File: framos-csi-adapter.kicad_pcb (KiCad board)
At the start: 4 copper layers, 26.5 x 26.5 mm, 41 parts, among them J1 DF40C-60DS-0.4V(51), J2 MSAK24025P30, U1 NTS0102DP, U2 NCP163ASN330T1G

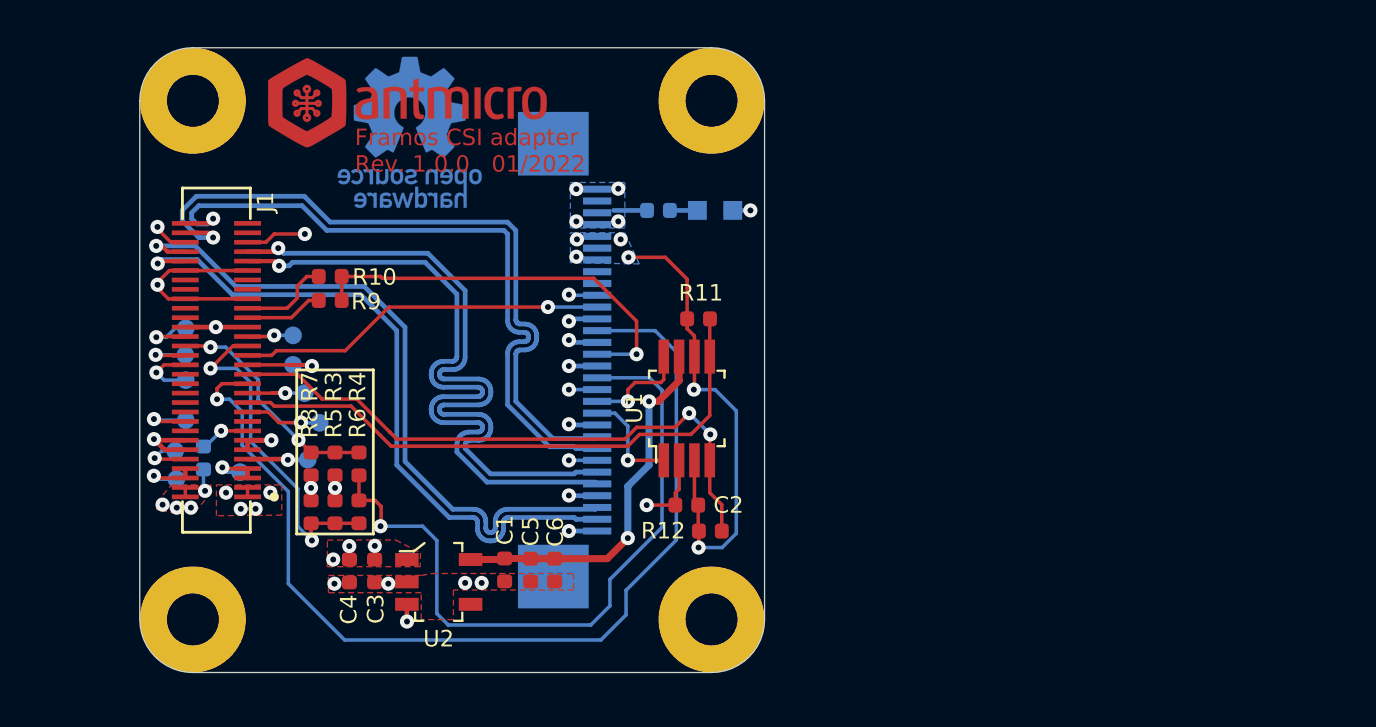
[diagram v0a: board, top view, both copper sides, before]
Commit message: Move R1 to top
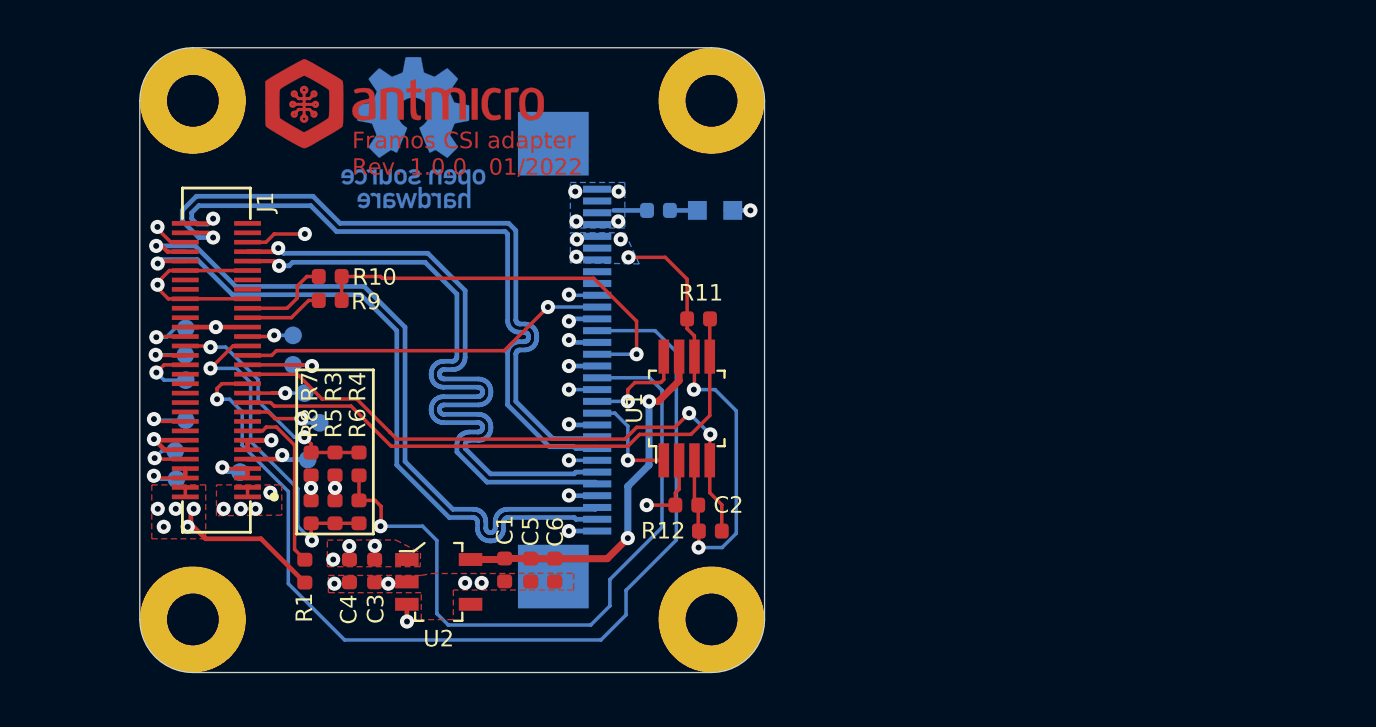
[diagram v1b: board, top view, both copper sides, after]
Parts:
- R1: moved to F.Cu
- moved R1 6.44 mm to (107.0, 122.2)
- moved N1 0.15 mm to (111.6, 103.6)
- moved N2 0.13 mm to (111.2, 102.4)
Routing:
- net 1V8_CAM: track 23.1 -> 28.7 mm, vias 11 -> 12
- net /XCLR: track 2.15 -> 7.42 mm, vias 1 -> 0

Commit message: Move power supply sections on PCB
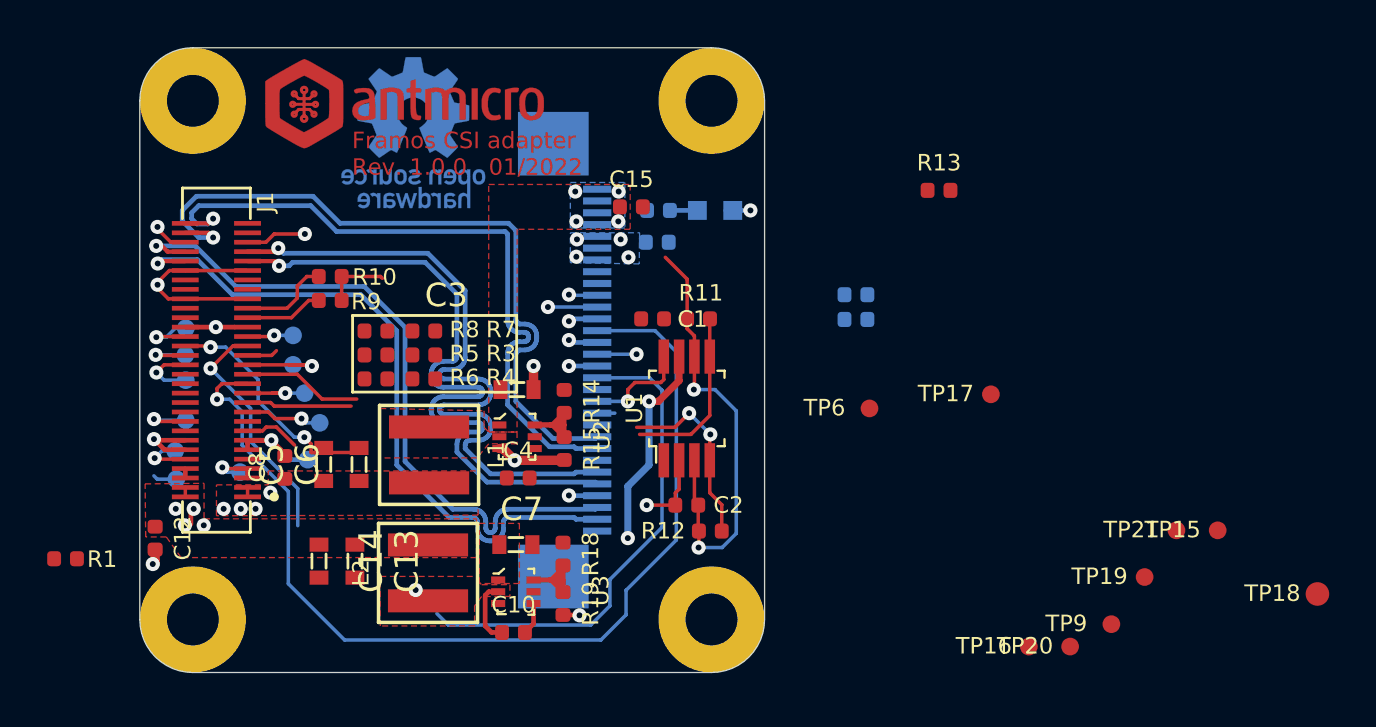
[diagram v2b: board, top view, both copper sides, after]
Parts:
- added C10: C_100n_0402, antmicro-footprints:0402-cap, F.Cu at (115.8, 124.8)
- added C12: C_100n_0402, framos-csi-adapter-footprints:0402-cap, F.Cu at (100.7, 120.8)
- added C13: C_22u_0603, antmicro-footprints:0603-cap, F.Cu at (109.1, 121.8)
- added C14: C_22u_0603, antmicro-footprints:0603-cap, F.Cu at (107.6, 121.8)
- added C15: C_100n_0402, framos-csi-adapter-footprints:0402-cap, F.Cu at (120.8, 106.8)
- added C16: C_100n_0402, framos-csi-adapter-footprints:0402-cap, B.Cu at (122.0, 108.2)
- added C7: C_22u_0603, antmicro-footprints:0603-cap, F.Cu at (116.0, 121.1)
- added C8: C_100n_0402, framos-csi-adapter-footprints:0402-cap, F.Cu at (106.2, 117.8)
- added L1: XEL4030-332MEC, antmicro-footprints:Coilcraft-XEL4030, F.Cu at (112.3, 117.3)
- added L2: XEL4030-222MEC, antmicro-footprints:Coilcraft-XEL4030, F.Cu at (112.2, 122.3)
- added R13: R_0R_0402, framos-csi-adapter-footprints:0402-res, F.Cu at (133.9, 106.0)
- added R14: R_14k7_0402, antmicro-footprints:0402-res, F.Cu at (118.0, 115.0)
- added R15: R_3k92_0402, antmicro-footprints:0402-res, F.Cu at (118.0, 117.0)
- added R16: R_0R_0402, antmicro-footprints:0402-res, B.Cu at (130.4, 110.5)
- added R17: R_0R_0402, antmicro-footprints:0402-res, B.Cu at (130.4, 111.5)
- added R18: R_12k4_0402, antmicro-footprints:0402-res, F.Cu at (118.0, 121.5)
- added R19: R_10k_0402, antmicro-footprints:0402-res, F.Cu at (118.0, 123.6)
- added TP15: TP_SMD_0_75MM, framos-csi-adapter-footprints:Testpoint_smd_0_75mm, F.Cu at (145.7, 120.5)
- added TP16: TP_SMD_0_75MM, framos-csi-adapter-footprints:Testpoint_smd_0_75mm, F.Cu at (137.7, 125.5)
- added TP17: TP_SMD_0_75MM, framos-csi-adapter-footprints:Testpoint_smd_0_75mm, F.Cu at (136.1, 114.8)
- added TP18: TP_SMD1MM, antmicro-footprints:Testpoint_smd_1mm, F.Cu at (149.9, 123.2)
- added TP19: TP_SMD_0_75MM, framos-csi-adapter-footprints:Testpoint_smd_0_75mm, F.Cu at (142.6, 122.5)
- added TP20: TP_SMD_0_75MM, framos-csi-adapter-footprints:Testpoint_smd_0_75mm, F.Cu at (139.5, 125.5)
- added TP21: TP_SMD_0_75MM, framos-csi-adapter-footprints:Testpoint_smd_0_75mm, F.Cu at (144.0, 120.5)
- added TP6: TP_SMD_0_75MM, framos-csi-adapter-footprints:Testpoint_smd_0_75mm, F.Cu at (130.9, 115.3)
- added TP9: TP_SMD_0_75MM, framos-csi-adapter-footprints:Testpoint_smd_0_75mm, F.Cu at (141.2, 124.5)
- added U3: AP62301Z6-7, antmicro-footprints:SOT-563, F.Cu at (116.0, 123.1)
- C3, C6: value C_1u_0402 -> C_22u_0603; footprint framos-csi-adapter-footprints:0402-cap -> antmicro-footprints:0603-cap
- C4: footprint framos-csi-adapter-footprints:0402-cap -> antmicro-footprints:0402-cap
- C5: value C_100n_0402 -> C_22u_0603; footprint framos-csi-adapter-footprints:0402-cap -> antmicro-footprints:0603-cap
- U2: value NCP163ASN330T1G -> AP62301Z6-7; footprint framos-csi-adapter-footprints:SOT-23-5 -> antmicro-footprints:SOT-563
- moved C1 12.4 mm to (121.8, 111.5), turned to 180 degrees
- moved R1 10.2 mm to (96.8, 121.7), turned to 180 degrees
- moved C5 9.86 mm to (107.8, 117.7), turned to 90 degrees
- moved C3 9.78 mm to (116.0, 114.5), turned to 0 degrees
- moved C6 9.43 mm to (109.3, 117.7), turned to 90 degrees
- moved C4 8.17 mm to (116.0, 118.2), turned to 0 degrees
- moved R8 8.15 mm to (110.0, 112.0), turned to 180 degrees
- moved R7 7.39 mm to (112.0, 112.0), turned to 180 degrees
- moved U2 7.00 mm to (116.0, 116.5)
- moved R5 6.88 mm to (110.0, 113.0), turned to 180 degrees
- moved R3 5.96 mm to (112.0, 113.0), turned to 180 degrees
- moved R6 5.68 mm to (110.0, 114.0), turned to 180 degrees
- moved R4 4.54 mm to (112.0, 114.0), turned to 0 degrees
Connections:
- C1 pad 1: 3V3 -> 3V3FFC
- C3 pad 1: 3V8_CAM -> 5V0_SYS
- C4 pad 1: 3V8_CAM -> Net-(C4-Pad1)
- C4 pad 2: GND -> Net-(C4-Pad2)
- C5 pad 1: 3V3 -> 3V8_CAM
- C6 pad 1: 3V3 -> 3V8_CAM
- J1 pad 16: Net-(J1-Pad16) -> (no net)
- J1 pad 17: Net-(J1-Pad17) -> (no net)
- J1 pad 20: Net-(J1-Pad20) -> (no net)
- J1 pad 22: Net-(J1-Pad22) -> (no net)
- J1 pad 24: Net-(J1-Pad24) -> (no net)
- J1 pad 26: Net-(J1-Pad26) -> (no net)
- J1 pad 28: Net-(J1-Pad28) -> (no net)
- J1 pad 40: Net-(J1-Pad40) -> (no net)
- J1 pad 42: Net-(J1-Pad42) -> (no net)
- J1 pad 45: Net-(J1-Pad45) -> (no net)
- J1 pad 46: Net-(J1-Pad46) -> CSI_D3_N
- J1 pad 47: Net-(J1-Pad47) -> (no net)
- J1 pad 48: Net-(J1-Pad48) -> CSI_D3_P
- J1 pad 57: Net-(J1-Pad57) -> CSI_D2_N
- J1 pad 59: Net-(J1-Pad59) -> CSI_D2_P
- J2 pad 11: CAM_SDA_3V3 -> CSI_D0_N
- J2 pad 12: CAM_SCL_3V3 -> CSI_D0_P
- J2 pad 14: CSI_CAM_EN -> CSI_CLK_N
- J2 pad 15: GND -> CSI_CLK_P
- J2 pad 16: CSI_CAM_CLK -> GND
- J2 pad 17: GND -> CAM_SDA_3V3
- J2 pad 18: CSI_CAM_XVS -> CAM_SCL_3V3
- J2 pad 2: CSI_D1_N -> CSI_D3_N
- J2 pad 20: CSI_CAM_XTRIG -> CSI_CAM_EN
- J2 pad 21: GND -> CSI_CAM_XVS
- J2 pad 22: Net-(J2-Pad22) -> CSI_CAM_CLK
- J2 pad 23: Net-(J2-Pad23) -> CSI_CAM_XTRIG
- J2 pad 24: 1V8_CAM -> 3V3FFC
- J2 pad 25: 1V8_CAM -> 3V3FFC
- J2 pad 26: 1V8_CAM -> 3V3FFC
- J2 pad 27: 3V8_CAM -> 5V0_SYS
- J2 pad 28: 3V8_CAM -> 5V0_SYS
- J2 pad 29: 3V8_CAM -> 5V0_SYS
- J2 pad 3: CSI_D1_P -> CSI_D3_P
- J2 pad 30: 3V8_CAM -> 5V0_SYS
- J2 pad 5: CSI_D0_N -> CSI_D2_N
- J2 pad 6: CSI_D0_P -> CSI_D2_P
- J2 pad 8: CSI_CLK_N -> CSI_D1_N
- J2 pad 9: CSI_CLK_P -> CSI_D1_P
- R10 pad 1: CSI_CAM_CLK -> Net-(R10-Pad1)
- R9 pad 1: CSI_CAM_CLK -> Net-(R10-Pad1)
- U1 pad 7: 3V3 -> 3V3FFC
- U2 pad 1: 3V8_CAM -> 5V0_SYS
- U2 pad 2: GND -> Net-(C4-Pad1)
- U2 pad 3: 3V8_CAM -> GND
- U2 pad 4: (no net) -> Net-(C4-Pad2)
- U2 pad 5: 3V3 -> Net-(TP6-Pad1)
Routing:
- net CSI_CAM_EN: track 29.6 -> 2.09 mm
- net 3V3: track 22.9 -> 0.00 mm, vias 2 -> 0
- net CSI_CLK_N: track 29.6 -> 50.5 mm
- net CSI_CAM_CLK: track 17.4 -> 0.00 mm, vias 1 -> 0
- net CSI_CAM_XTRIG: track 15.7 -> 1.31 mm, vias 1 -> 0
- net CAM_SCL_1V8: track 25.0 -> 11.9 mm
- net CAM_SDA_1V8: track 25.9 -> 13.1 mm
- net 3V3FFC: track 0.00 -> 8.84 mm, vias 0 -> 6
- net 1V8_CAM: track 28.7 -> 20.2 mm, vias 12 -> 6
- net Net-(R14-Pad2): track 0.00 -> 5.81 mm
- net /XCLR: track 7.42 -> 2.38 mm
- net Net-(R18-Pad2): track 0.00 -> 4.99 mm
- net /PW_EN_0: track 14.5 -> 10.2 mm, vias 2 -> 1
- net Net-(C10-Pad1): track 0.00 -> 3.44 mm, vias 0 -> 1
- net CAM_SDA_3V3: track 4.50 -> 1.24 mm
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- added copper zone on B.Cu, net 3V3FFC
- added copper zone on B.Cu, net 5V0_SYS
- added copper zone on F.Cu, net 5V0_SYS
- added copper zone on F.Cu, net Net-(C10-Pad1)
- added copper zone on F.Cu, net Net-(C4-Pad1)
- removed copper zone on B.Cu, net 1V8_CAM
- removed copper zone on B.Cu, net 3V8_CAM
- removed copper zone on F.Cu, net GND

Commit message: Layout, tunning
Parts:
- removed N1: oshw_logo, framos-csi-adapter-footprints:oshw-logo
- added REF**: OSHW-Logo2_7.3x6mm_Copper_Mask, framos-csi-adapter-footprints:OSHW-Logo2_7.3x6mm_Copper_Mask, F.Cu at (123.6, 119.0)
- added REF**: OSHW-Logo2_7.3x6mm_Copper, framos-csi-adapter-footprints:OSHW-Logo2_7.3x6mm_Copper, F.Cu at (123.6, 119.0)
- added REF**: MSAK24025P30_PLUG, framos-csi-adapter-footprints:MSAK24025P30_PLUG, F.Cu at (113.2, 114.1)
- added kibuzzard-621A77E1: G***, label, F.Cu at (102.0, 110.4)
- C10, C4: footprint antmicro-footprints:0402-cap -> framos-csi-adapter-footprints:0402-cap
- C12, C8, J1, MP1, MP2, MP3, MP4, R1, TP15, TP16: moved to B.Cu
- C13, C14, C3, C5, C6, C7: footprint antmicro-footprints:0603-cap -> framos-csi-adapter-footprints:0603-cap
- C16, D1, J2, R2: moved to F.Cu
- L1: value XEL4030-332MEC -> 74479887222C; footprint antmicro-footprints:Coilcraft-XEL4030 -> framos-csi-adapter-footprints:L_1008_2520Metric
- L2: value XEL4030-222MEC -> 74479887222C; footprint antmicro-footprints:Coilcraft-XEL4030 -> framos-csi-adapter-footprints:L_1008_2520Metric
- R14: value R_14k7_0402 -> R_37k4_0402; footprint antmicro-footprints:0402-res -> framos-csi-adapter-footprints:0402-res
- R15: value R_3k92_0402 -> R_10k_0402; footprint antmicro-footprints:0402-res -> framos-csi-adapter-footprints:0402-res
- R16, R17: footprint antmicro-footprints:0402-res -> framos-csi-adapter-footprints:0402-res; moved to F.Cu
- R18, R19: footprint antmicro-footprints:0402-res -> framos-csi-adapter-footprints:0402-res
- TP18: footprint antmicro-footprints:Testpoint_smd_1mm -> framos-csi-adapter-footprints:Testpoint_smd_1mm
- U2, U3: footprint antmicro-footprints:SOT-563 -> framos-csi-adapter-footprints:SOT-563
- moved TP9 42.0 mm to (102.7, 107.8)
- moved TP21 39.1 mm to (105.2, 114.9)
- moved TP18 37.1 mm to (112.9, 122.5), turned to 270 degrees
- moved TP15 34.4 mm to (114.5, 106.1)
- moved R13 32.6 mm to (101.3, 107.6), turned to 180 degrees
- moved TP20 32.6 mm to (108.7, 114.8)
- moved R1 31.8 mm to (121.4, 101.4), turned to 90 degrees
- moved TP16 31.5 mm to (112.8, 106.2)
- moved MP2 31.1 mm to (124.2, 102.2), turned to 270 degrees
- moved MP3 31.1 mm to (102.2, 124.2), turned to 270 degrees
- moved TP6 29.6 mm to (101.8, 120.3), turned to 270 degrees
- moved TP19 29.1 mm to (113.7, 125.8), turned to 270 degrees
- moved TP17 27.1 mm to (109.2, 117.7)
- moved C12 26.5 mm to (121.5, 104.4)
- moved TP11 24.4 mm to (118.5, 100.7), turned to 90 degrees
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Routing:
- net CSI_CAM_XVS: track 44.0 -> 12.6 mm, vias 2 -> 3
- net CSI_CLK_N: track 50.5 -> 23.5 mm
- net /PW_EN_1: track 9.98 -> 35.3 mm, vias 2 -> 3
- net CSI_D2_P: track 0.00 -> 24.0 mm, vias 0 -> 1
- net CSI_D2_N: track 0.00 -> 24.0 mm, vias 0 -> 1
- net CSI_D3_P: track 0.00 -> 23.5 mm, vias 0 -> 1
- net CSI_D3_N: track 0.00 -> 23.5 mm, vias 0 -> 1
- net /INCK: track 3.33 -> 18.7 mm, vias 0 -> 1
- net /MCLK1: track 3.88 -> 18.5 mm, vias 0 -> 1
- net CAM_SCL_3V3: track 4.48 -> 18.0 mm, vias 1 -> 0
- net CAM_SDA_3V3: track 1.24 -> 13.9 mm, vias 1 -> 2
- net CSI_CAM_XTRIG: track 1.31 -> 13.8 mm, vias 0 -> 1
- net CSI_CAM_CLK: track 0.00 -> 12.5 mm
- net CAM_SCL_1V8: track 11.9 -> 23.1 mm, vias 0 -> 1
- net 3V8_CAM: track 0.40 -> 10.1 mm, vias 4 -> 8
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- added copper zone on B.Cu, net 1V8_CAM
- added copper zone on F.Cu, net 3V3FFC
- added copper zone on B.Cu, net 3V8_CAM
- added copper zone on In1.Cu, net 5V0_SYS
- added copper zone on B.Cu, net GND
- added copper zone on F.Cu, net GND
- removed copper zone on B.Cu, net 3V3FFC
- removed copper zone on B.Cu, net 5V0_SYS
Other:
- board text added: "Framos CSI adapter Rev. 1.0.0 02/2022"
- board text removed: "Framos CSI adapter Rev. 1.0.0 01/2022"
- board text removed: "HOST"
- board text removed: "POWER"

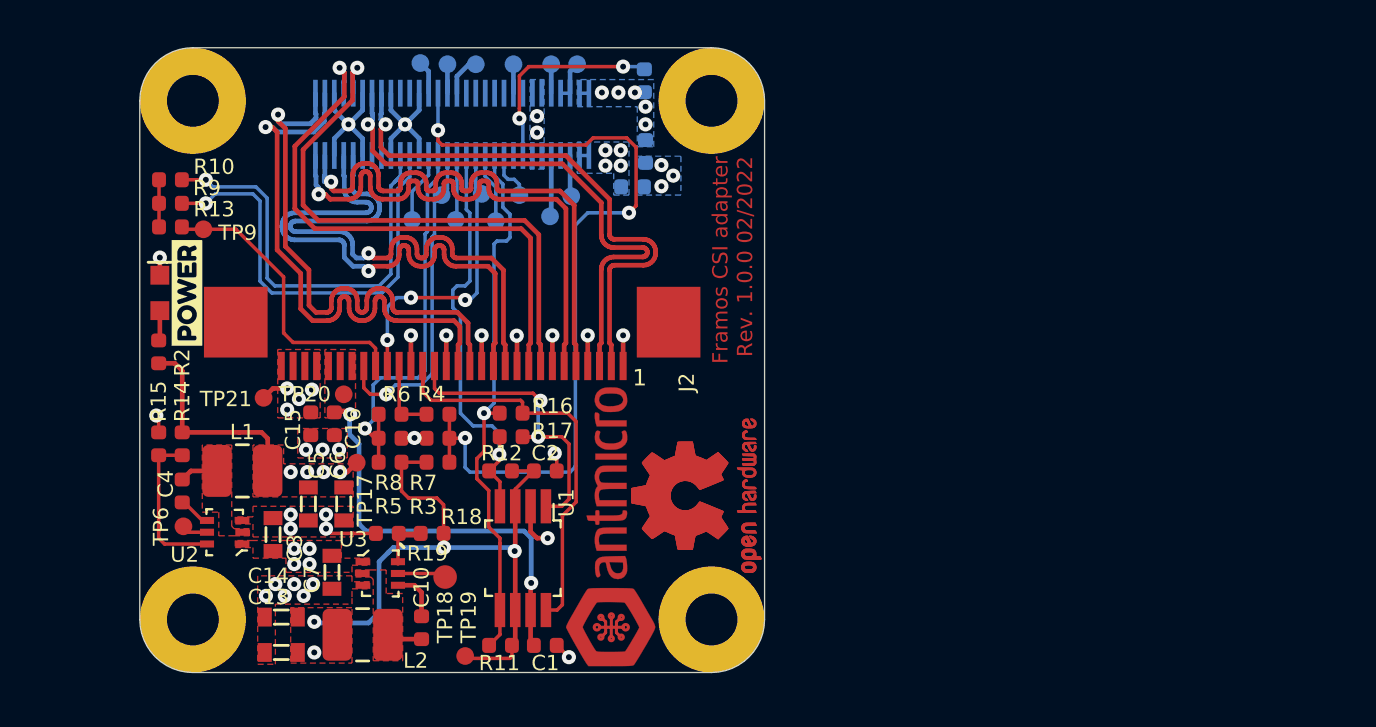
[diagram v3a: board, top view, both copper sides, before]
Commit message: Changed voltage translator to XSON8 package. Crossed P and N signals on D2 and D3 lanes
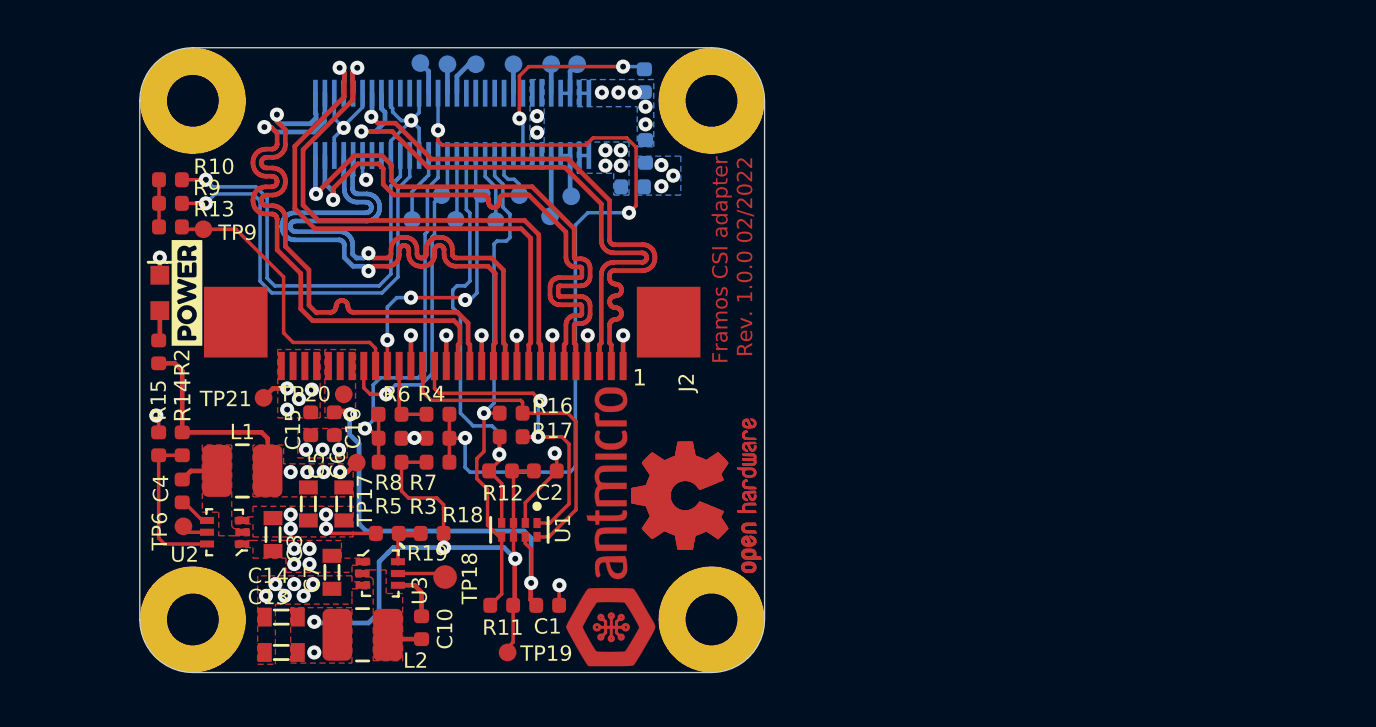
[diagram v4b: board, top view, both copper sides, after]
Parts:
- U1: value NTS0102DP -> NTS0102GT; footprint framos-csi-adapter-footprints:TSSOP-8_W3mm -> antmicro-footprints:PSON50P100X195X50-8N
- moved TP19 1.81 mm to (115.5, 125.7)
- moved C1 1.70 mm to (117.3, 123.7)
- moved R11 1.70 mm to (115.3, 123.7)
- moved U1 1.21 mm to (116.1, 120.5), turned to 270 degrees
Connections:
- J1 pad 16: (no net) -> Net-(J1-Pad16)
- J1 pad 17: (no net) -> Net-(J1-Pad17)
- J1 pad 20: (no net) -> Net-(J1-Pad20)
- J1 pad 22: (no net) -> Net-(J1-Pad22)
- J1 pad 24: (no net) -> Net-(J1-Pad24)
- J1 pad 26: (no net) -> Net-(J1-Pad26)
- J1 pad 28: (no net) -> Net-(J1-Pad28)
- J1 pad 40: (no net) -> Net-(J1-Pad40)
- J1 pad 42: (no net) -> Net-(J1-Pad42)
- J1 pad 45: (no net) -> Net-(J1-Pad45)
- J1 pad 46: CSI_D3_N -> CSI_D3_P
- J1 pad 47: (no net) -> Net-(J1-Pad47)
- J1 pad 48: CSI_D3_P -> CSI_D3_N
- J1 pad 57: CSI_D2_N -> CSI_D2_P
- J1 pad 59: CSI_D2_P -> CSI_D2_N
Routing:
- net CAM_SCL_3V3: track 18.0 -> 15.0 mm
- net 1V8_CAM: track 29.4 -> 27.1 mm
- net CAM_SCL_1V8: track 23.1 -> 21.5 mm
- net GND: track 29.9 -> 31.0 mm
- net CAM_SDA_3V3: track 13.9 -> 14.7 mm
- net CAM_SDA_1V8: track 17.9 -> 18.6 mm
- net CSI_CLK_N: track 23.5 -> 24.1 mm
- net CSI_D3_N: track 23.5 -> 24.0 mm
- net CSI_D3_P: track 23.5 -> 24.0 mm
